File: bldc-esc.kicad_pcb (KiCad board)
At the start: 4 copper layers, 116 x 112 mm, 449 parts, among them J101 XT60PW-M, J102 MT60 / 12AWG pigtail, J103 CHASSIS, J301 DUMP RESISTOR, J401 USB4105-GF-A, J501 SWD / KEY 7, J601 HALL, J602 ENCODER, J701 CAN, J702 UART / 3V3, J703 HW ENABLE, J801 THROTTLE_ADC, J802 AUX_ANALOG_ADC, J803 RC PWM, J804 BRAKE / DIR, J805 NTC_MOTOR, J806 NTC_DUMP, Q201 ISC011N06LM5, Q202 ISC011N06LM5, Q203 ISC011N06LM5, Q204 ISC011N06LM5, Q205 ISC011N06LM5, Q206 ISC011N06LM5, Q301 ISC011N06LM5, Q302 2N7002, SW501 RESET, SW502 USER, U101 TLV9024PWR, U102 TLV9024PWR, U201 DRV8353SRTAT, U202 INA241A2IDR, U203 INA241A2IDR, U204 INA241A2IDR, U301 TLV3011BIDBVR, U302 UCC27511ADBVR, U303 INA180A1IDBVR, U304 TLV3201AIDBVR, U305 TPS3808G50DBVR, U306 SN74LVC1G17DBVR, U307 SN74LVC1G74DCTR, U308 REF2025AIDDCR, U401 LM5164DDAR, U402 TPS2116DRLR, U403 TLV75801PDRVR, U404 USBLC6-2SC6, U501 STM32G474VET6, U502 REF2025AIDDCR, U503 M24C64-RMN6TP, U601 TPS2553DBVR-1, U602 TPS2553DBVR-1, U603 SN74LVC3G17DCTR, U604 SN74LVC3G17DCTR, U701 TPS389033DSER, U702 TPS3431SDRBR, U703 SN74LVC1G11DBVR, U704 SN74LVC1G11DBVR, U705 SN74LVC1G74DCTR, U706 SN74LVC244APWR, U707 SN74LVC1G11DBVR, U708 SN74LVC1G11DBVR, U709 TCAN3403DRQ1, U710 SN74LVC1G14DBVR, U711 SN74LVC1G11DBVR, U712 SN74LVC1G11DBVR, U801 TLV9064IPWR, U802 SN74LVC3G17DCTR, U803 TLV9062IDR, U804 TLV9062IDR, Y501 8MHz / CL18p

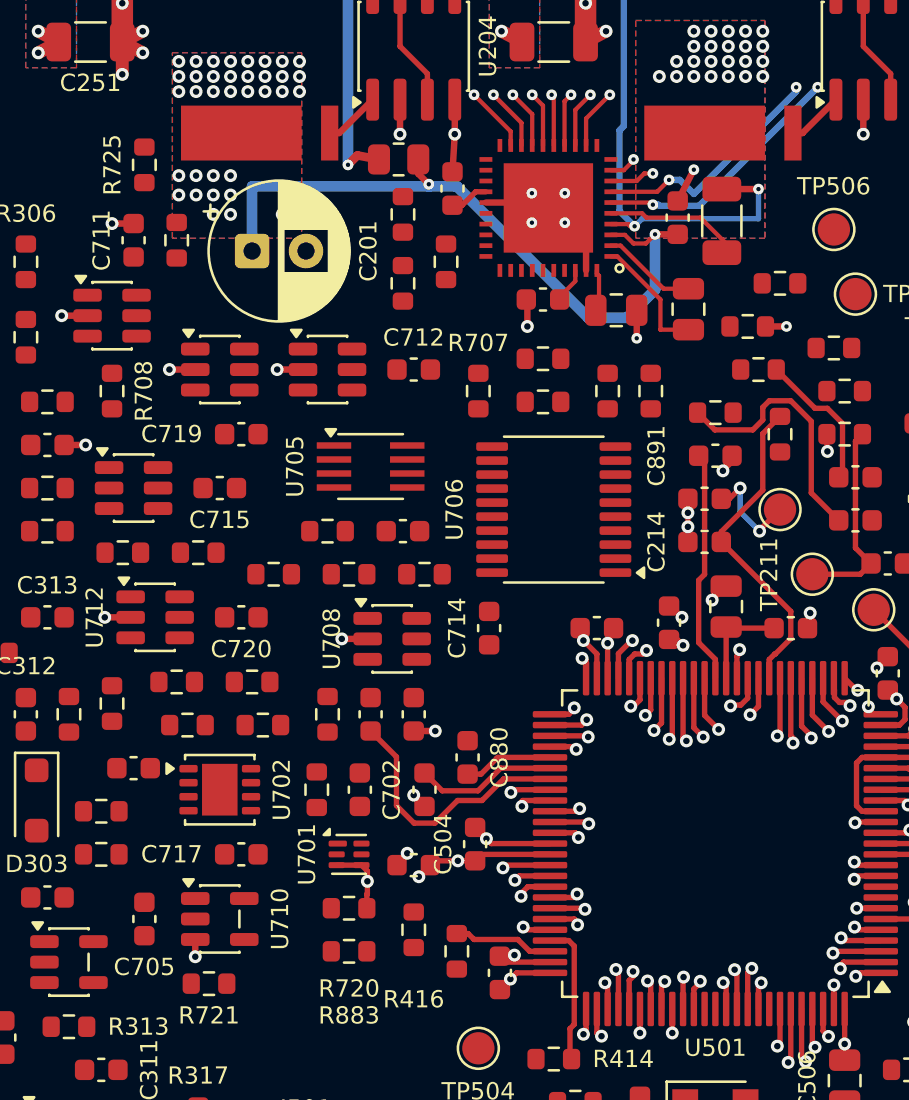
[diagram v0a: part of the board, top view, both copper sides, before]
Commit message: route pwm and driver controls
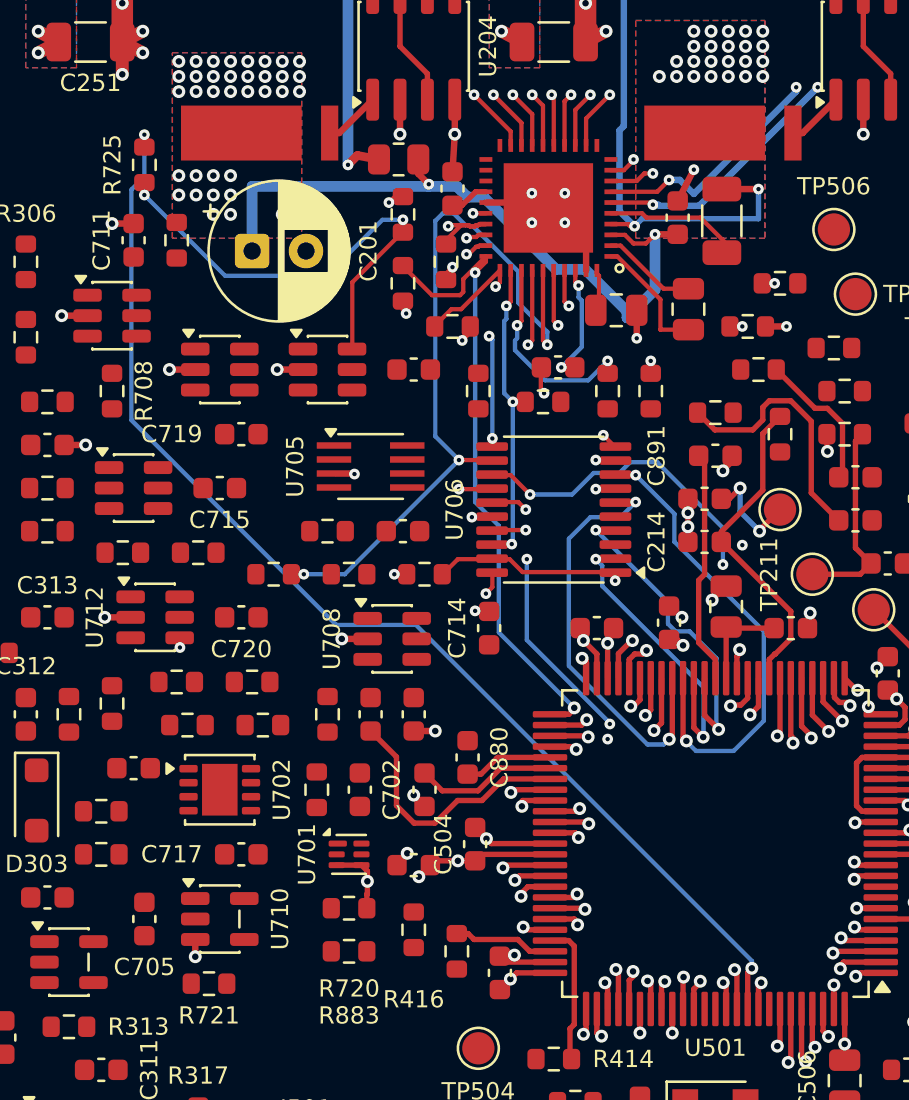
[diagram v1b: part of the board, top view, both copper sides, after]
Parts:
- moved R204 4.46 mm to (120.8, 90.5)
- moved C206 3.23 mm to (125.7, 92.4)
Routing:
- net DRV_nFAULT_SENSE: track 1.97 -> 55.6 mm, vias 1 -> 2
- net DRV_SDO: track 1.79 -> 54.4 mm, vias 1 -> 2
- net DRV_SDI: track 1.27 -> 48.1 mm, vias 1 -> 2
- net DRV_SCK: track 1.82 -> 42.9 mm, vias 1 -> 2
- net IN_BL: track 0.00 -> 35.7 mm, vias 0 -> 3
- net IN_CL: track 0.00 -> 33.1 mm, vias 0 -> 3
- net PWM_CH: track 1.83 -> 32.0 mm, vias 1 -> 5
- net DRV_nCS: track 1.28 -> 29.9 mm, vias 1 -> 2
- net DRV_ENABLE: track 0.00 -> 28.2 mm, vias 0 -> 2
- net DRV_nFAULT: track 0.00 -> 26.2 mm, vias 0 -> 3
- net IN_CH: track 0.00 -> 24.6 mm, vias 0 -> 3
- net IN_BH: track 0.00 -> 24.2 mm, vias 0 -> 3
- net /09_safety/nPWM_ENABLE: track 0.00 -> 24.1 mm, vias 0 -> 2
- net PWM_CL: track 2.57 -> 26.3 mm, vias 1 -> 3
- net IN_AL: track 0.00 -> 20.4 mm, vias 0 -> 3
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
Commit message: route safety logic and analog power
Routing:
- net 3V3: track 40.8 -> 233.1 mm, vias 21 -> 38
- net NRST: track 2.13 -> 178.4 mm, vias 2 -> 9
- net 3V3_A: track 27.7 -> 127.3 mm, vias 2 -> 13
- net BRK_ARMED: track 0.00 -> 90.9 mm, vias 0 -> 7
- net /16_supervisor/nHW_ENABLE_IN: track 0.00 -> 80.9 mm, vias 0 -> 1
- net nOC_HW: track 30.7 -> 105.3 mm, vias 0 -> 11
- net BUS_OK: track 5.59 -> 74.8 mm, vias 0 -> 2
- net WD_RUN: track 0.00 -> 65.3 mm, vias 0 -> 3
- net HW_ENABLE_OK: track 0.00 -> 48.0 mm, vias 0 -> 2
- net DRV_WAKE_REQ: track 1.11 -> 46.4 mm, vias 1 -> 2
- net nHW_ENABLE_FILT: track 0.00 -> 44.1 mm, vias 0 -> 2
- net BRIDGE_ARM_REQ: track 1.38 -> 44.8 mm, vias 1 -> 4
- net WD_RUN_SENSE: track 1.27 -> 38.3 mm, vias 1 -> 5
- net DUMP_PWM: track 1.83 -> 37.0 mm, vias 1 -> 3
- net nHW_ENABLE_SENSE: track 2.04 -> 36.4 mm, vias 1 -> 7
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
